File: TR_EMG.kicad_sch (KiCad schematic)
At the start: 7 parts, among them J1 1727230, J2 1844236, J3 1727230, J4 1727230, J5 1727230, J6 1727230, J7 1727230

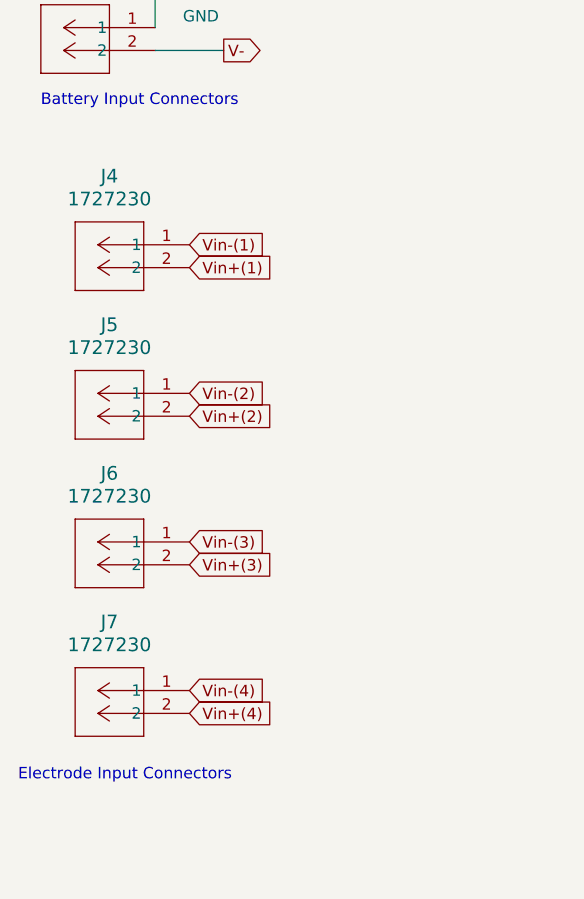
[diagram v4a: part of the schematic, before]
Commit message: removed sda scl pullups, removed electrode connectors to make space for proper connectors later
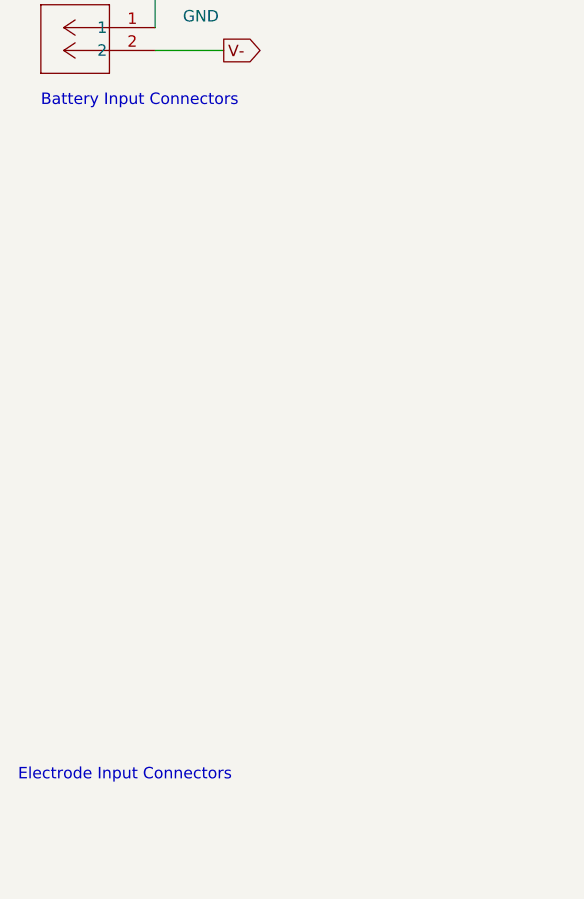
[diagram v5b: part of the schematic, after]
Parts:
- removed J4, J5, J6, J7: 1727230, CONN_1727230_PXC, symbol 1727230:1727230
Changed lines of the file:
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@@
-    )
-  )
-  (global_label "Vin+(3)" (shape input) (at 34.29 100.33 0) (fields_autoplaced)
-    (effects (font (size 1.27 1.27)) (justify left))
-    (property "Intersheetrefs" "${INTERSHEET_REFS}" (at 44.5929 100.33 0)
-      (effects (font (size 1.27 1.27)) (justify left) hide)
     )
   )
@@
     )
   )
-  (global_label "Vin+(2)" (shape input) (at 34.29 83.82 0) (fields_autoplaced)
-    (effects (font (size 1.27 1.27)) (justify left))
-    (property "Intersheetrefs" "${INTERSHEET_REFS}" (at 44.5929 83.82 0)
-      (effects (font (size 1.27 1.27)) (justify left) hide)
-    )
-  )
   (global_label "V-" (shape output) (at 38.1 43.18 0) (fields_autoplaced)
     (effects (font (size 1.27 1.27)) (justify left))
     (property "Intersheetrefs" "${INTERSHEET_REFS}" (at 43.7462 43.18 0)
-      (effects (font (size 1.27 1.27)) (justify left) hide)
-    )
-  )
-  (global_label "Vin-(2)" (shape input) (at 34.29 81.28 0) (fields_autoplaced)
-    (effects (font (size 1.27 1.27)) (justify left))
-    (property "Intersheetrefs" "${INTERSHEET_REFS}" (at 44.5929 81.28 0)
       (effects (font (size 1.27 1.27)) (justify left) hide)
     )
@@
     )
   )
-  (global_label "Vin+(1)" (shape input) (at 34.29 67.31 0) (fields_autoplaced)
-    (effects (font (size 1.27 1.27)) (justify left))
-    (property "Intersheetrefs" "${INTERSHEET_REFS}" (at 44.5929 67.31 0)
-      (effects (font (size 1.27 1.27)) (justify left) hide)
-    )
-  )
   (global_label "Vin+(1)" (shape input) (at 157.48 41.91 180) (fields_autoplaced)
     (effects (font (size 1.27 1.27)) (justify right))
     (property "Intersheetrefs" "${INTERSHEET_REFS}" (at 147.1771 41.91 0)
       (effects (font (size 1.27 1.27)) (justify right) hide)
-    )
-  )
-  (global_label "Vin-(3)" (shape input) (at 34.29 97.79 0) (fields_autoplaced)
-    (effects (font (size 1.27 1.27)) (justify left))
-    (property "Intersheetrefs" "${INTERSHEET_REFS}" (at 44.5929 97.79 0)
-      (effects (font (size 1.27 1.27)) (justify left) hide)
     )
   )
@@
     )
   )
-  (global_label "Vin+(4)" (shape input) (at 34.29 116.84 0) (fields_autoplaced)
-    (effects (font (size 1.27 1.27)) (justify left))
-    (property "Intersheetrefs" "${INTERSHEET_REFS}" (at 44.5929 116.84 0)
-      (effects (font (size 1.27 1.27)) (justify left) hide)
-    )
-  )
   (global_label "V-" (shape input) (at 187.96 143.51 270) (fields_autoplaced)
     (effects (font (size 1.27 1.27)) (justify right))
     (property "Intersheetrefs" "${INTERSHEET_REFS}" (at 187.96 149.1562 90)
       (effects (font (size 1.27 1.27)) (justify right) hide)
-    )
-  )
-  (global_label "Vin-(1)" (shape input) (at 34.29 64.77 0) (fields_autoplaced)
-    (effects (font (size 1.27 1.27)) (justify left))
-    (property "Intersheetrefs" "${INTERSHEET_REFS}" (at 44.5929 64.77 0)
-      (effects (font (size 1.27 1.27)) (justify left) hide)
     )
   )
@@
     )
   )
-  (global_label "Vin-(4)" (shape input) (at 34.29 114.3 0) (fields_autoplaced)
-    (effects (font (size 1.27 1.27)) (justify left))
-    (property "Intersheetrefs" "${INTERSHEET_REFS}" (at 44.5929 114.3 0)
-      (effects (font (size 1.27 1.27)) (justify left) hide)
-    )
-  )
   (global_label "Vin+(3)" (shape input) (at 157.48 105.41 180) (fields_autoplaced)
     (effects (font (size 1.27 1.27)) (justify right))
     (property "Intersheetrefs" "${INTERSHEET_REFS}" (at 147.1771 105.41 0)
       (effects (font (size 1.27 1.27)) (justify right) hide)
-    )
-  )
-  (symbol (lib_id "1727230:1727230") (at 34.29 64.77 0) (mirror y) (unit 1)
-    (in_bom yes) (on_board yes) (dnp no) (fields_autoplaced)
-    (property "Reference" "J4" (at 25.4 57.15 0)
-      (effects (font (size 1.524 1.524)))
-    )
-    (property "Value" "1727230" (at 25.4 59.69 0)
-      (effects (font (size 1.524 1.524)))
-    )
-    (property "Footprint" "CONN_1727230_PXC" (at 34.29 64.77 0)
-      (effects (font (size 1.27 1.27) italic) hide)
-    )
-    (property "Datasheet" "1727230" (at 34.29 64.77 0)
-      (effects (font (size 1.27 1.27) italic) hide)
-    )
-    (pin "2")
-    (pin "1")
-    (instances
-      (project "TR_EMG"
-        (path "/c6167f6f-8a8c-40a1-9c06-7f0e8ea44639"
-          (reference "J4") (unit 1)
-        )
-      )
     )
   )
@@
         )
       )
-    )
-  )
-  (symbol (lib_id "1727230:1727230") (at 34.29 97.79 0) (mirror y) (unit 1)
-    (in_bom yes) (on_board yes) (dnp no) (fields_autoplaced)
-    (property "Reference" "J6" (at 25.4 90.17 0)
-      (effects (font (size 1.524 1.524)))
-    )
-    (property "Value" "1727230" (at 25.4 92.71 0)
-      (effects (font (size 1.524 1.524)))
-    )
-    (property "Footprint" "CONN_1727230_PXC" (at 34.29 97.79 0)
-      (effects (font (size 1.27 1.27) italic) hide)
-    )
-    (property "Datasheet" "1727230" (at 34.29 97.79 0)
-      (effects (font (size 1.27 1.27) italic) hide)
-    )
-    (pin "2")
-    (pin "1")
-    (instances
-      (project "TR_EMG"
-        (path "/c6167f6f-8a8c-40a1-9c06-7f0e8ea44639"
-          (reference "J6") (unit 1)
-        )
-      )
-    )
-  )
-  (symbol (lib_id "1727230:1727230") (at 34.29 81.28 0) (mirror y) (unit 1)
-    (in_bom yes) (on_board yes) (dnp no) (fields_autoplaced)
-    (property "Reference" "J5" (at 25.4 73.66 0)
-      (effects (font (size 1.524 1.524)))
-    )
-    (property "Value" "1727230" (at 25.4 76.2 0)
-      (effects (font (size 1.524 1.524)))
-    )
-    (property "Footprint" "CONN_1727230_PXC" (at 34.29 81.28 0)
-      (effects (font (size 1.27 1.27) italic) hide)
-    )
-    (property "Datasheet" "1727230" (at 34.29 81.28 0)
-      (effects (font (size 1.27 1.27) italic) hide)
-    )
-    (pin "2")
-    (pin "1")
-    (instances
-      (project "TR_EMG"
-        (path "/c6167f6f-8a8c-40a1-9c06-7f0e8ea44639"
-          (reference "J5") (unit 1)
-        )
-      )
-    )
-  )
-  (symbol (lib_id "1727230:1727230") (at 34.29 114.3 0) (mirror y) (unit 1)
-    (in_bom yes) (on_board yes) (dnp no) (fields_autoplaced)
-    (property "Reference" "J7" (at 25.4 106.68 0)
-      (effects (font (size 1.524 1.524)))
-    )
-    (property "Value" "1727230" (at 25.4 109.22 0)
-      (effects (font (size 1.524 1.524)))
-    )
-    (property "Footprint" "CONN_1727230_PXC" (at 34.29 114.3 0)
-      (effects (font (size 1.27 1.27) italic) hide)
-    )
-    (property "Datasheet" "1727230" (at 34.29 114.3 0)
-      (effects (font (size 1.27 1.27) italic) hide)
-    )
-    (pin "2")
-    (pin "1")
-    (instances
-      (project "TR_EMG"
-        (path "/c6167f6f-8a8c-40a1-9c06-7f0e8ea44639"
-          (reference "J7") (unit 1)
-        )
-      )

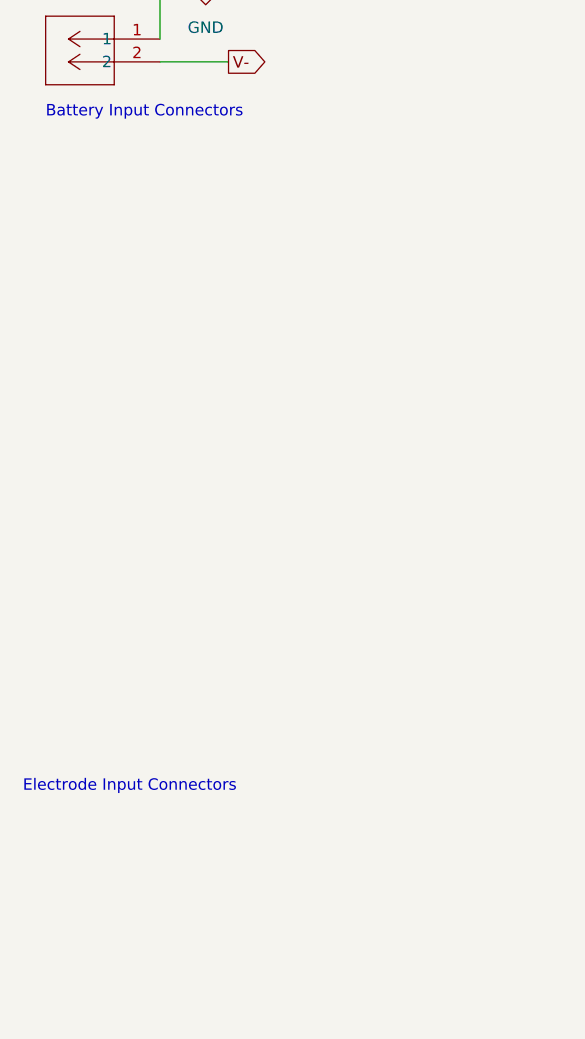
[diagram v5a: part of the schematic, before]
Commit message: added audio jack connectors for emg connections
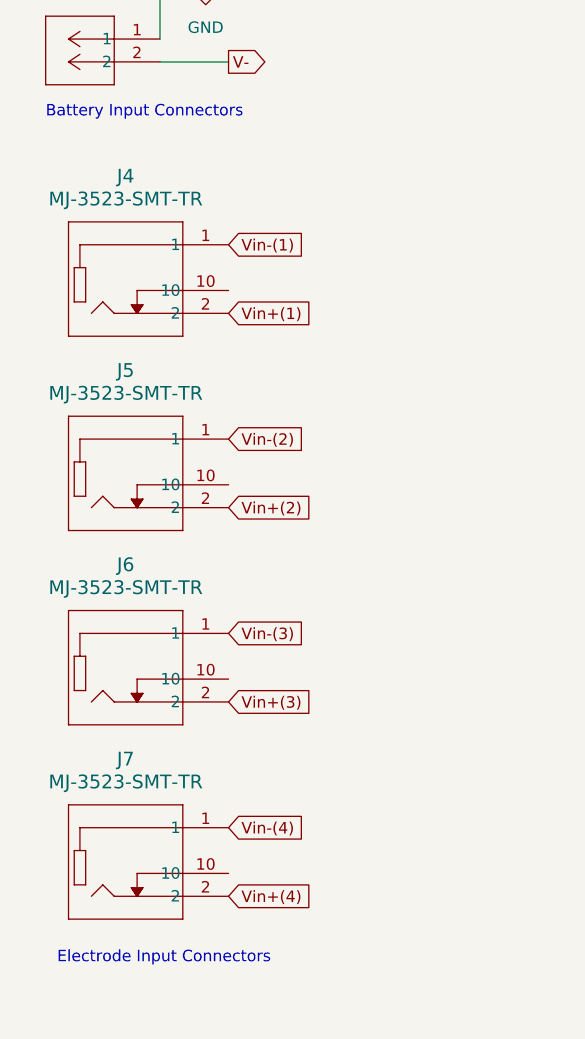
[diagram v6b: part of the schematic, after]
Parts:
- added J4, J5, J6, J7: MJ-3523-SMT-TR, CONN_MJ-3523_CUD, symbol MJ_3523_SMT_TR:MJ-3523-SMT-TR
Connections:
- net Vin+(1): now also J4.2
- net Vin+(2): now also J5.2
- net Vin+(3): now also J6.2
- net Vin+(4): now also J7.2
- net Vin-(1): now also J4.1
- net Vin-(2): now also J5.1
- net Vin-(3): now also J6.1
- net Vin-(4): now also J7.1
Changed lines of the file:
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@@
     (stroke (width 0) (type default))
   )
-  (text "Electrode Input Connectors" (at 15.24 124.46 0)
+  (text "Electrode Input Connectors" (at 19.05 143.51 0)
     (effects (font (size 1.27 1.27)) (justify left bottom))
   )
@@
     )
   )
+  (global_label "Vin-(1)" (shape input) (at 38.1 63.5 0) (fields_autoplaced)
+    (effects (font (size 1.27 1.27)) (justify left))
+    (property "Intersheetrefs" "${INTERSHEET_REFS}" (at 48.4029 63.5 0)
+      (effects (font (size 1.27 1.27)) (justify left) hide)
+    )
+  )
+  (global_label "Vin+(3)" (shape input) (at 38.1 114.3 0) (fields_autoplaced)
+    (effects (font (size 1.27 1.27)) (justify left))
+    (property "Intersheetrefs" "${INTERSHEET_REFS}" (at 48.4029 114.3 0)
+      (effects (font (size 1.27 1.27)) (justify left) hide)
+    )
+  )
   (global_label "V-" (shape output) (at 38.1 43.18 0) (fields_autoplaced)
     (effects (font (size 1.27 1.27)) (justify left))
@@
     )
   )
+  (global_label "Vin-(2)" (shape input) (at 38.1 85.09 0) (fields_autoplaced)
+    (effects (font (size 1.27 1.27)) (justify left))
+    (property "Intersheetrefs" "${INTERSHEET_REFS}" (at 48.4029 85.09 0)
+      (effects (font (size 1.27 1.27)) (justify left) hide)
+    )
+  )
   (global_label "V-" (shape input) (at 187.96 80.01 270) (fields_autoplaced)
     (effects (font (size 1.27 1.27)) (justify right))
@@
     )
   )
+  (global_label "Vin-(3)" (shape input) (at 38.1 106.68 0) (fields_autoplaced)
+    (effects (font (size 1.27 1.27)) (justify left))
+    (property "Intersheetrefs" "${INTERSHEET_REFS}" (at 48.4029 106.68 0)
+      (effects (font (size 1.27 1.27)) (justify left) hide)
+    )
+  )
   (global_label "Vin+(1)" (shape input) (at 157.48 41.91 180) (fields_autoplaced)
     (effects (font (size 1.27 1.27)) (justify right))
@@
     )
   )
+  (global_label "Vin+(4)" (shape input) (at 38.1 135.89 0) (fields_autoplaced)
+    (effects (font (size 1.27 1.27)) (justify left))
+    (property "Intersheetrefs" "${INTERSHEET_REFS}" (at 48.4029 135.89 0)
+      (effects (font (size 1.27 1.27)) (justify left) hide)
+    )
+  )
   (global_label "V-" (shape input) (at 187.96 143.51 270) (fields_autoplaced)
     (effects (font (size 1.27 1.27)) (justify right))
@@
     )
   )
+  (global_label "Vin-(4)" (shape input) (at 38.1 128.27 0) (fields_autoplaced)
+    (effects (font (size 1.27 1.27)) (justify left))
+    (property "Intersheetrefs" "${INTERSHEET_REFS}" (at 48.4029 128.27 0)
+      (effects (font (size 1.27 1.27)) (justify left) hide)
+    )
+  )
+  (global_label "Vin+(1)" (shape input) (at 38.1 71.12 0) (fields_autoplaced)
+    (effects (font (size 1.27 1.27)) (justify left))
+    (property "Intersheetrefs" "${INTERSHEET_REFS}" (at 48.4029 71.12 0)
+      (effects (font (size 1.27 1.27)) (justify left) hide)
+    )
+  )
   (global_label "V+" (shape input) (at 187.96 60.96 90) (fields_autoplaced)
     (effects (font (size 1.27 1.27)) (justify left))
@@
     )
   )
+  (global_label "Vin+(2)" (shape input) (at 38.1 92.71 0) (fields_autoplaced)
+    (effects (font (size 1.27 1.27)) (justify left))
+    (property "Intersheetrefs" "${INTERSHEET_REFS}" (at 48.4029 92.71 0)
+      (effects (font (size 1.27 1.27)) (justify left) hide)
+    )
+  )
   (global_label "Vin+(3)" (shape input) (at 157.48 105.41 180) (fields_autoplaced)
     (effects (font (size 1.27 1.27)) (justify right))
     (property "Intersheetrefs" "${INTERSHEET_REFS}" (at 147.1771 105.41 0)
       (effects (font (size 1.27 1.27)) (justify right) hide)
+    )
+  )
+  (symbol (lib_id "MJ_3523_SMT_TR:MJ-3523-SMT-TR") (at 38.1 85.09 0) (unit 1)
+    (in_bom yes) (on_board yes) (dnp no) (fields_autoplaced)
+    (property "Reference" "J5" (at 26.67 77.47 0)
+      (effects (font (size 1.524 1.524)))
+    )
+    (property "Value" "MJ-3523-SMT-TR" (at 26.67 80.01 0)
+      (effects (font (size 1.524 1.524)))
+    )
+    (property "Footprint" "CONN_MJ-3523_CUD" (at 38.1 85.09 0)
+      (effects (font (size 1.27 1.27) italic) hide)
+    )
+    (property "Datasheet" "MJ-3523-SMT-TR" (at 38.1 85.09 0)
+      (effects (font (size 1.27 1.27) italic) hide)
+    )
+    (pin "2")
+    (pin "1")
+    (pin "10")
+    (instances
+      (project "TR_EMG"
+        (path "/c6167f6f-8a8c-40a1-9c06-7f0e8ea44639"
+          (reference "J5") (unit 1)
+        )
+      )
     )
   )
@@
         (path "/c6167f6f-8a8c-40a1-9c06-7f0e8ea44639"
           (reference "J3") (unit 1)
+        )
+      )
+    )
+  )
+  (symbol (lib_id "MJ_3523_SMT_TR:MJ-3523-SMT-TR") (at 38.1 106.68 0) (unit 1)
+    (in_bom yes) (on_board yes) (dnp no) (fields_autoplaced)
+    (property "Reference" "J6" (at 26.67 99.06 0)
+      (effects (font (size 1.524 1.524)))
+    )
+    (property "Value" "MJ-3523-SMT-TR" (at 26.67 101.6 0)
+      (effects (font (size 1.524 1.524)))
+    )
+    (property "Footprint" "CONN_MJ-3523_CUD" (at 38.1 106.68 0)
+      (effects (font (size 1.27 1.27) italic) hide)
+    )
+    (property "Datasheet" "MJ-3523-SMT-TR" (at 38.1 106.68 0)
+      (effects (font (size 1.27 1.27) italic) hide)
+    )
+    (pin "2")
+    (pin "1")
+    (pin "10")
+    (instances
+      (project "TR_EMG"
+        (path "/c6167f6f-8a8c-40a1-9c06-7f0e8ea44639"
+          (reference "J6") (unit 1)
+        )
+      )
+    )
+  )
+  (symbol (lib_id "MJ_3523_SMT_TR:MJ-3523-SMT-TR") (at 38.1 63.5 0) (unit 1)
+    (in_bom yes) (on_board yes) (dnp no) (fields_autoplaced)
+    (property "Reference" "J4" (at 26.67 55.88 0)
+      (effects (font (size 1.524 1.524)))
+    )
+    (property "Value" "MJ-3523-SMT-TR" (at 26.67 58.42 0)
+      (effects (font (size 1.524 1.524)))
+    )
+    (property "Footprint" "CONN_MJ-3523_CUD" (at 38.1 63.5 0)
+      (effects (font (size 1.27 1.27) italic) hide)
+    )
+    (property "Datasheet" "MJ-3523-SMT-TR" (at 38.1 63.5 0)
+      (effects (font (size 1.27 1.27) italic) hide)
+    )
+    (pin "2")
+    (pin "1")
+    (pin "10")
+    (instances
+      (project "TR_EMG"
+        (path "/c6167f6f-8a8c-40a1-9c06-7f0e8ea44639"
+          (reference "J4") (unit 1)
         )
       )
@@
         )
       )
+    )
+  )
+  (symbol (lib_id "MJ_3523_SMT_TR:MJ-3523-SMT-TR") (at 38.1 128.27 0) (unit 1)
+    (in_bom yes) (on_board yes) (dnp no) (fields_autoplaced)
+    (property "Reference" "J7" (at 26.67 120.65 0)
+      (effects (font (size 1.524 1.524)))
+    )
+    (property "Value" "MJ-3523-SMT-TR" (at 26.67 123.19 0)
+      (effects (font (size 1.524 1.524)))
+    )
+    (property "Footprint" "CONN_MJ-3523_CUD" (at 38.1 128.27 0)
+      (effects (font (size 1.27 1.27) italic) hide)
+    )
+    (property "Datasheet" "MJ-3523-SMT-TR" (at 38.1 128.27 0)
+      (effects (font (size 1.27 1.27) italic) hide)
+    )
+    (pin "2")
+    (pin "1")
+    (pin "10")
+    (instances
+      (project "TR_EMG"
+        (path "/c6167f6f-8a8c-40a1-9c06-7f0e8ea44639"
+          (reference "J7") (unit 1)
+        )
+      )
